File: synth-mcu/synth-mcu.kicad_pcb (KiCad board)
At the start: 2 copper layers, 60 x 70 mm, 5 parts, among them J1 LoopMatrix, J2 AudioControls, J3 Conn_01x25_Socket, J4 Conn_01x25_Socket, J5 AUXOut

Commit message: add mounting holes to mcu pcb
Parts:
- added H1: MountingHole, MountingHole:MountingHole_3.2mm_M3, F.Cu at (88.0, 31.0)
- added H2: MountingHole, MountingHole:MountingHole_3.2mm_M3, F.Cu at (22.0, 31.0)
- added H3: MountingHole, MountingHole:MountingHole_3.2mm_M3, F.Cu at (88.0, 93.0)
- added H4: MountingHole, MountingHole:MountingHole_3.2mm_M3, F.Cu at (22.0, 93.0)
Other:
- board size 60 x 70 mm -> 74 x 70 mm

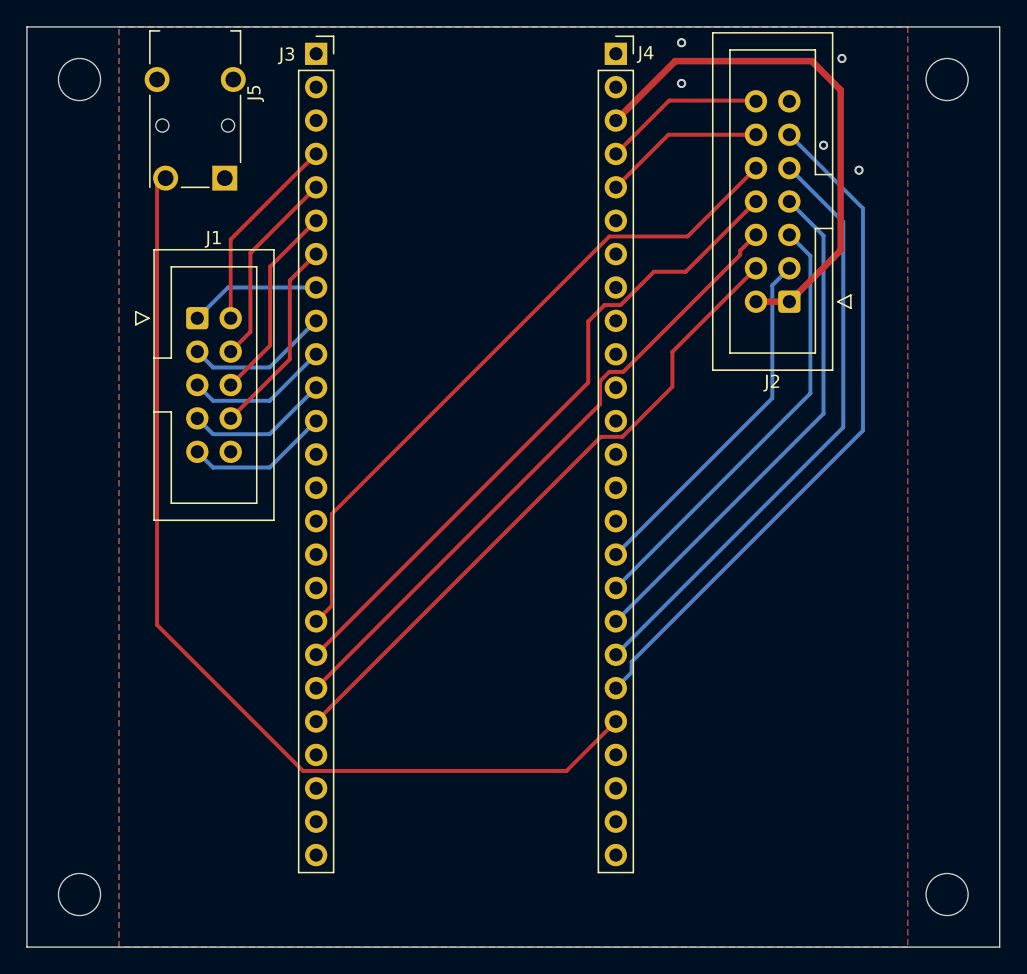
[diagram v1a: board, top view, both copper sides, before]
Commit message: GPIO breakout for MCU board
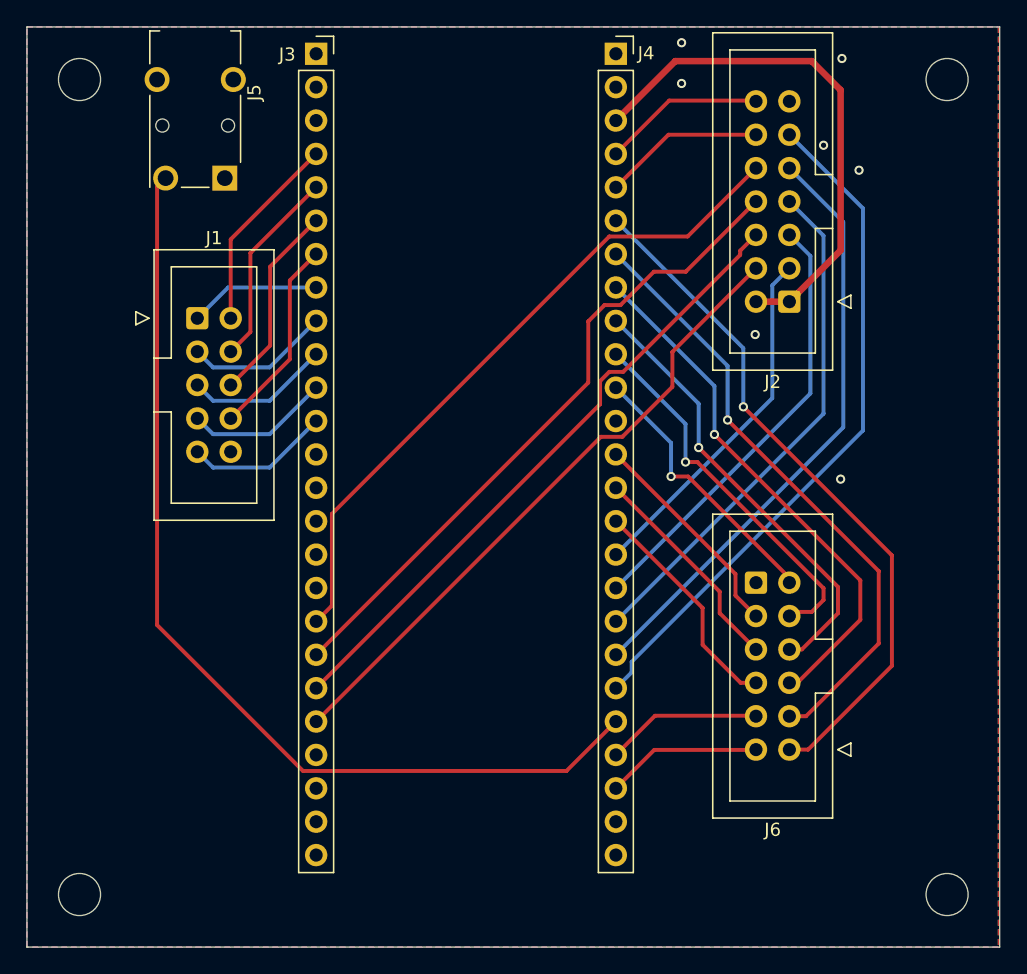
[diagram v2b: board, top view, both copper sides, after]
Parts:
- added J6: GPIO, Connector_IDC:IDC-Header_2x06_P2.54mm_Vertical, F.Cu at (76.0, 82.0)
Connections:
- J4 pad 10: unconnected-(J4-Pin_10-Pad10) -> /GPIO_9
- J4 pad 11: unconnected-(J4-Pin_11-Pad11) -> /GPIO_11
- J4 pad 13: unconnected-(J4-Pin_13-Pad13) -> /GPIO_10
- J4 pad 14: unconnected-(J4-Pin_14-Pad14) -> /GPIO_8
- J4 pad 15: unconnected-(J4-Pin_15-Pad15) -> /GPIO_6
- J4 pad 22: unconnected-(J4-Pin_22-Pad22) -> /GPIO_4
- J4 pad 23: unconnected-(J4-Pin_23-Pad23) -> /GPIO_2
- J4 pad 6: unconnected-(J4-Pin_6-Pad6) -> /GPIO_1
- J4 pad 7: unconnected-(J4-Pin_7-Pad7) -> /GPIO_3
- J4 pad 8: unconnected-(J4-Pin_8-Pad8) -> /GPIO_5
- J4 pad 9: unconnected-(J4-Pin_9-Pad9) -> /GPIO_7
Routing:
- net /GPIO_1: track 0.00 -> 53.0 mm, vias 0 -> 1
- net /GPIO_3: track 0.00 -> 47.0 mm, vias 0 -> 1
- net /GPIO_5: track 0.00 -> 40.4 mm, vias 0 -> 1
- net /GPIO_7: track 0.00 -> 34.1 mm, vias 0 -> 1
- net /GPIO_9: track 0.00 -> 28.9 mm, vias 0 -> 1
- net /GPIO_11: track 0.00 -> 21.1 mm, vias 0 -> 1
- net /GPIO_6: track 0.00 -> 17.4 mm
- net /GPIO_8: track 0.00 -> 16.7 mm
- net /GPIO_10: track 0.00 -> 16.7 mm
- net /GPIO_4: track 0.00 -> 11.9 mm
- net /GPIO_2: track 0.00 -> 11.9 mm
- net GND: vias 5 -> 7

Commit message: implement design suggestions from TA
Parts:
- removed J6: GPIO, Connector_IDC:IDC-Header_2x06_P2.54mm_Vertical
- added J7: GPIO, Connector_IDC:IDC-Header_2x07_P2.54mm_Vertical, F.Cu at (76.1, 82.0)

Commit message: Manufacturing changes & Gerber files
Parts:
- added J6: Conn_01x05, Connector_Molex:Molex_KK-254_AE-6410-05A_1x05_P2.54mm_Vertical, F.Cu at (32.9, 92.6)
- added J8: GPIO2, Connector_Molex:Molex_KK-254_AE-6410-05A_1x05_P2.54mm_Vertical, F.Cu at (22.2, 57.0)
- J5: footprint Connector_Audio:Jack_3.5mm_Switronic_ST-005-G_horizontal -> Library:AudioConnector_2092-STX-3000-ND
- moved J5 12.5 mm to (31.4, 44.5), turned to 180 degrees
- moved J7 2.50 mm to (76.1, 84.5)
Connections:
- J3 pad 13: unconnected-(J3-Pin_13-Pad13) -> /GPIO2_1
- J3 pad 14: unconnected-(J3-Pin_14-Pad14) -> /GPIO2_2
- J3 pad 15: unconnected-(J3-Pin_15-Pad15) -> /GPIO2_3
- J3 pad 16: unconnected-(J3-Pin_16-Pad16) -> /GPIO2_4
- J3 pad 17: unconnected-(J3-Pin_17-Pad17) -> /LED_4
- J3 pad 22: unconnected-(J3-Pin_22-Pad22) -> /LED_1
- J3 pad 23: unconnected-(J3-Pin_23-Pad23) -> /LED_2
- J3 pad 24: unconnected-(J3-Pin_24-Pad24) -> /LED_3
- J4 pad 12: unconnected-(J4-Pin_12-Pad12) -> /GPIO_13
- J4 pad 24: unconnected-(J4-Pin_24-Pad24) -> /GPIO_12
- J5 pad S: /DAC_SPEAKER -> GND
- J5 pad T: GND -> /DAC_SPEAKER
- J7 pad 1: /GPIO_1 -> GND
- J7 pad 10: /GPIO_10 -> /GPIO_8
- J7 pad 11: /GPIO_11 -> /GPIO_9
- J7 pad 12: /GPIO_12 -> /GPIO_10
- J7 pad 13: /GPIO_13 -> /GPIO_11
- J7 pad 14: GND -> /GPIO_12
- J7 pad 2: /GPIO_2 -> /GPIO_13
- J7 pad 3: /GPIO_3 -> /GPIO_1
- J7 pad 4: /GPIO_4 -> /GPIO_2
- J7 pad 5: /GPIO_5 -> /GPIO_3
- J7 pad 6: /GPIO_6 -> /GPIO_4
- J7 pad 7: /GPIO_7 -> /GPIO_5
- J7 pad 8: /GPIO_8 -> /GPIO_6
- J7 pad 9: /GPIO_9 -> /GPIO_7
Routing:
- net /GPIO_13: track 0.00 -> 50.8 mm
- net /LED_4: track 0.00 -> 32.8 mm
- net /GPIO_12: track 0.00 -> 24.3 mm
- net /GPIO2_1: track 0.00 -> 19.1 mm, vias 0 -> 2
- net /GPIO2_2: track 0.00 -> 17.9 mm, vias 0 -> 2
- net /GPIO2_4: track 0.00 -> 17.8 mm, vias 0 -> 2
- net /GPIO2_3: track 0.00 -> 17.8 mm, vias 0 -> 2
- net /DAC_SPEAKER: track 75.3 -> 83.7 mm
- net /LED_3: track 0.00 -> 7.80 mm
- net /LED_1: track 0.00 -> 7.01 mm
- net /LED_2: track 0.00 -> 7.01 mm
- net GND: vias 7 -> 13
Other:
- board text added: "Team PEAK - ECEN1400 100-1"
